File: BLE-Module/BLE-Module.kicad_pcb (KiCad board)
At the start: 2 copper layers, 50 x 31.4 mm, 20 parts, among them J1 USB-C

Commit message: Redesigned board
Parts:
- added C_OUT2: 22uF, Capacitor_SMD:C_1206_3216Metric, F.Cu at (190.9, 108.8)
- added ESP32_C_Power1: 22uF, Capacitor_SMD:C_1206_3216Metric, F.Cu at (168.9, 98.3)
- C_OUT1: value 52uF -> 22uF
- ESP32: value ESP32 -> ESP32-S3-MINI-1-N4R2
- moved J1 20.0 mm to (149.8, 106.6), turned to -90 degrees
- moved C3 12.9 mm to (159.4, 108.4)
- moved C4 12.9 mm to (159.4, 110.4)
- moved R4 12.9 mm to (159.4, 104.7)
- moved C_BYPASS1 12.9 mm to (159.4, 106.5)
- moved R3 11.1 mm to (159.4, 103.0), turned to 180 degrees
- moved BuckConverter1 11.1 mm to (161.1, 96.6), turned to 180 degrees
- moved R_FB_1 9.35 mm to (156.7, 94.8), turned to 90 degrees
- moved R_FB_2 4.68 mm to (190.9, 113.7), turned to 0 degrees
- moved R1 3.13 mm to (187.7, 113.9)
- moved ESP32 1.27 mm to (178.7, 101.6)
- moved C_OUT1 0.10 mm to (190.9, 111.5), turned to 0 degrees
- renumbered SW_BOOT1 to BOOT, SW_RST1 to RESET
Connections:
- net /+V_OUT renamed +3V3
- net VCC renamed +12V
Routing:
- net +3V3: track 63.4 -> 23.8 mm, vias 0 -> 7
- net /T1_IN: track 0.00 -> 22.5 mm
- net /R1_OUT: track 0.00 -> 19.1 mm
- net GND: track 0.00 -> 18.4 mm
- net Net-(UART-SERIAL1-V+): track 27.4 -> 12.7 mm, vias 2 -> 0
- net Net-(UART-SERIAL1-V-): track 30.0 -> 19.7 mm, vias 2 -> 0
- net /D+: track 19.9 -> 28.7 mm
- net /D-: track 19.6 -> 27.7 mm
- net Net-(J1-CC1): track 4.47 -> 8.30 mm
- net Net-(J1-CC2): track 10.0 -> 12.6 mm, vias 0 -> 2
- net /RESET: track 32.1 -> 30.6 mm
- net /LED: track 4.23 -> 3.27 mm
- net /BOOT: track 19.8 -> 20.0 mm, vias 0 -> 2

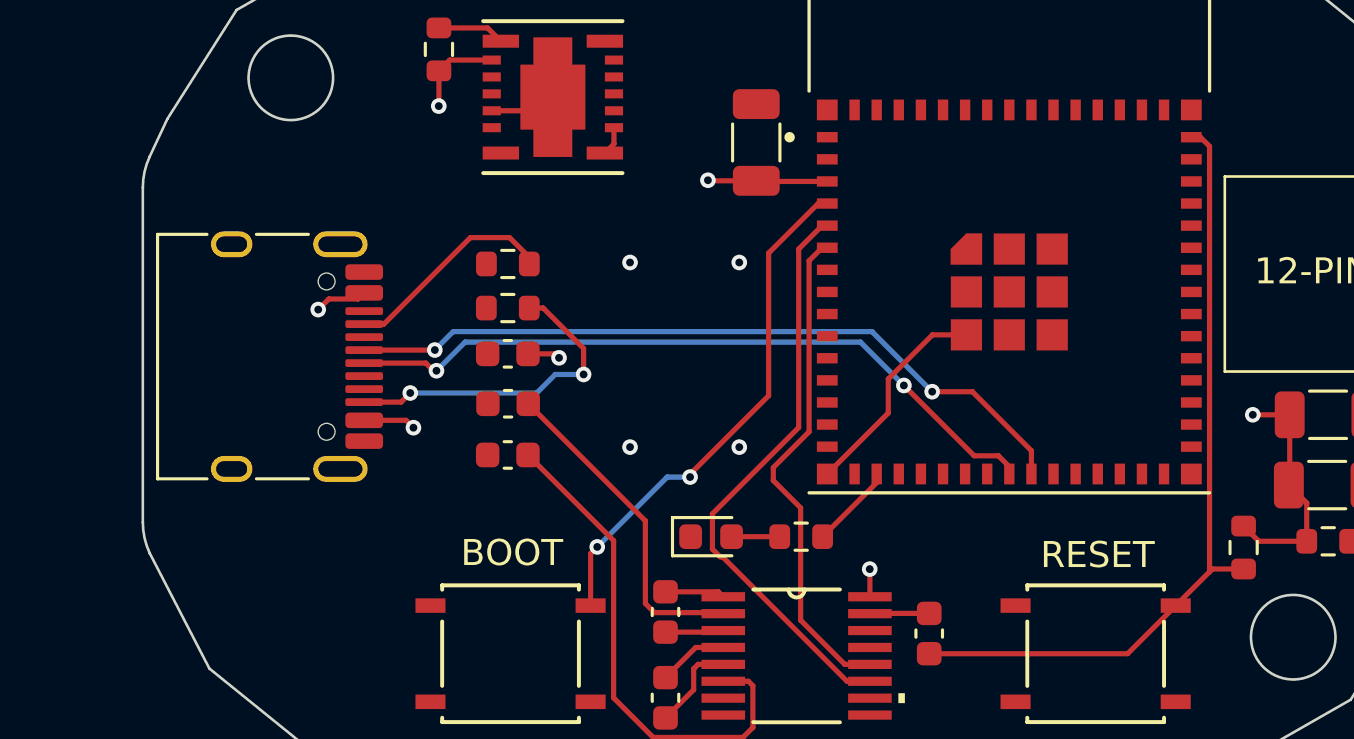
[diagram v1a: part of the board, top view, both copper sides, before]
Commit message: Picked USB-C receptacle
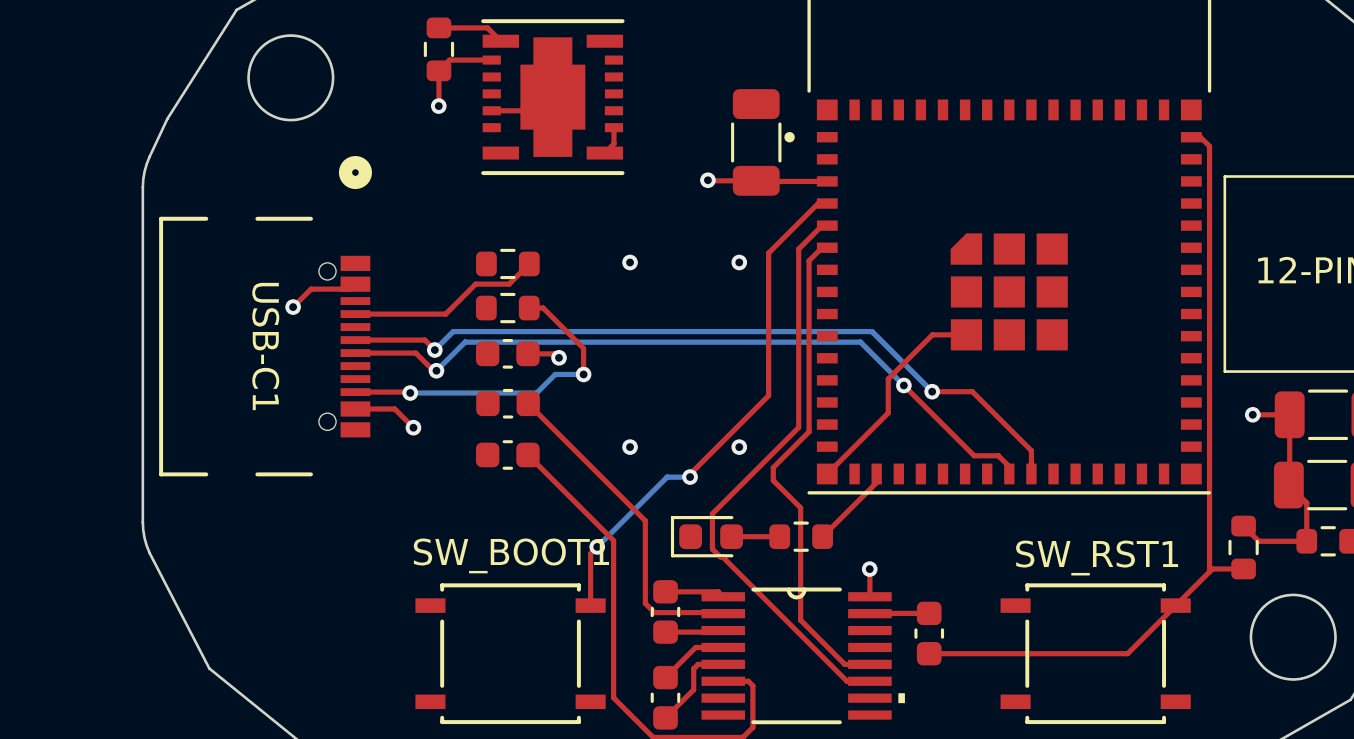
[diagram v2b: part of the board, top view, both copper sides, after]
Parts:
- removed J1: USB-C, Connector_USB:USB_C_Receptacle_HRO_TYPE-C-31-M-12
- added USB-C1: USB4105-GF-A, USB-C:USB4105_GCT, F.Cu at (150.1, 106.2)
- R2: value R -> 5.1K
- renumbered BOOT to SW_BOOT1, RESET to SW_RST1
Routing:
- net +3V3: track 23.8 -> 25.0 mm
- net Net-(USB-C1-CC1): track 8.30 -> 7.48 mm

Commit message: Added text and graphics
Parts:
- added G***: LOGO, LOGO, F.Cu at (152.0, 115.5)
- added G***: LOGO, LOGO, B.Cu at (170.7, 106.8)
- renumbered SW_BOOT1 to BOOT, SW_RST1 to RESET, USB-C1 to USB-C
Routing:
- net /RX_IN: track 0.00 -> 19.4 mm, vias 0 -> 3
- net +12V: track 1.12 -> 18.5 mm, vias 0 -> 3
- net /TX_OUT: track 0.00 -> 16.8 mm, vias 0 -> 3
- net GND: track 18.4 -> 22.8 mm, vias 0 -> 1
- net /BOOT: track 20.0 -> 20.5 mm
- net (no net): vias 4 -> 0
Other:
- board text added: "+12V"
- board text added: "GND"
- board text added: "RX"
- board text added: "TX"

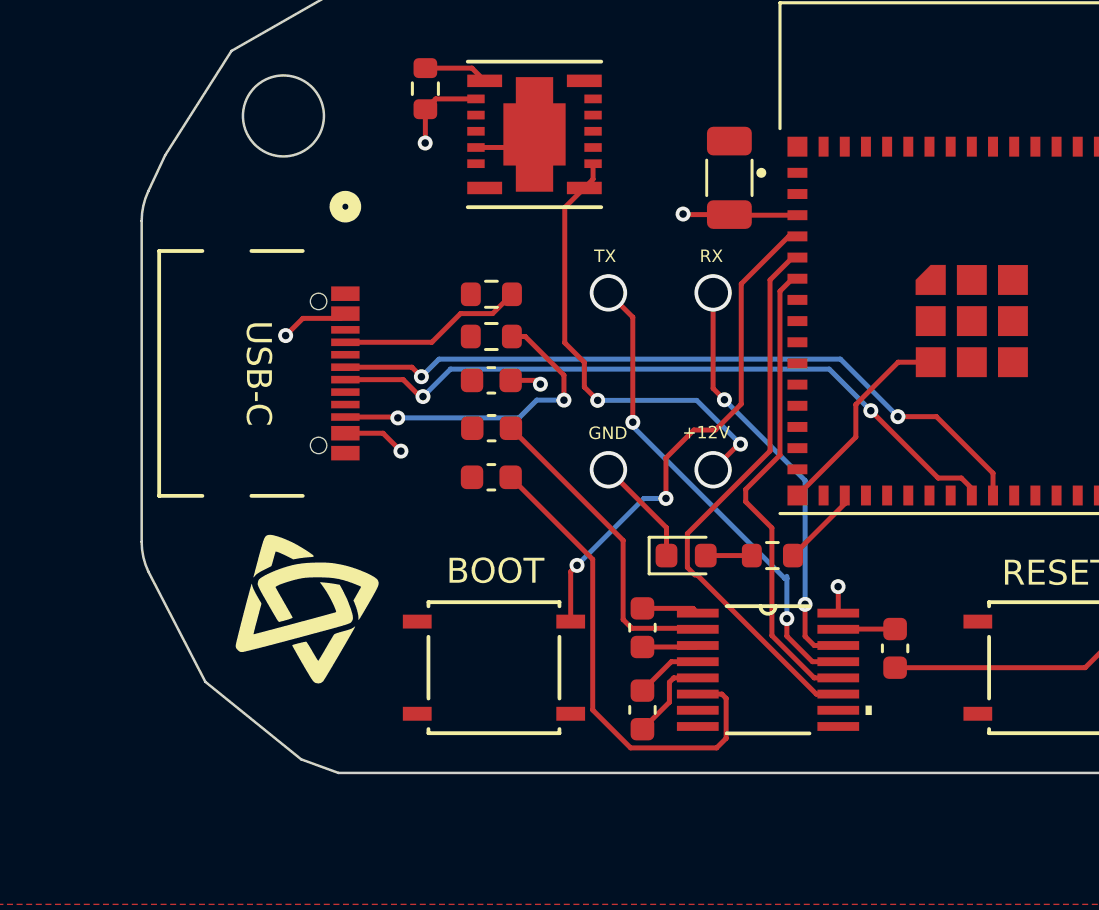
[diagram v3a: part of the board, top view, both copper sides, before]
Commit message: Added common-anode LED
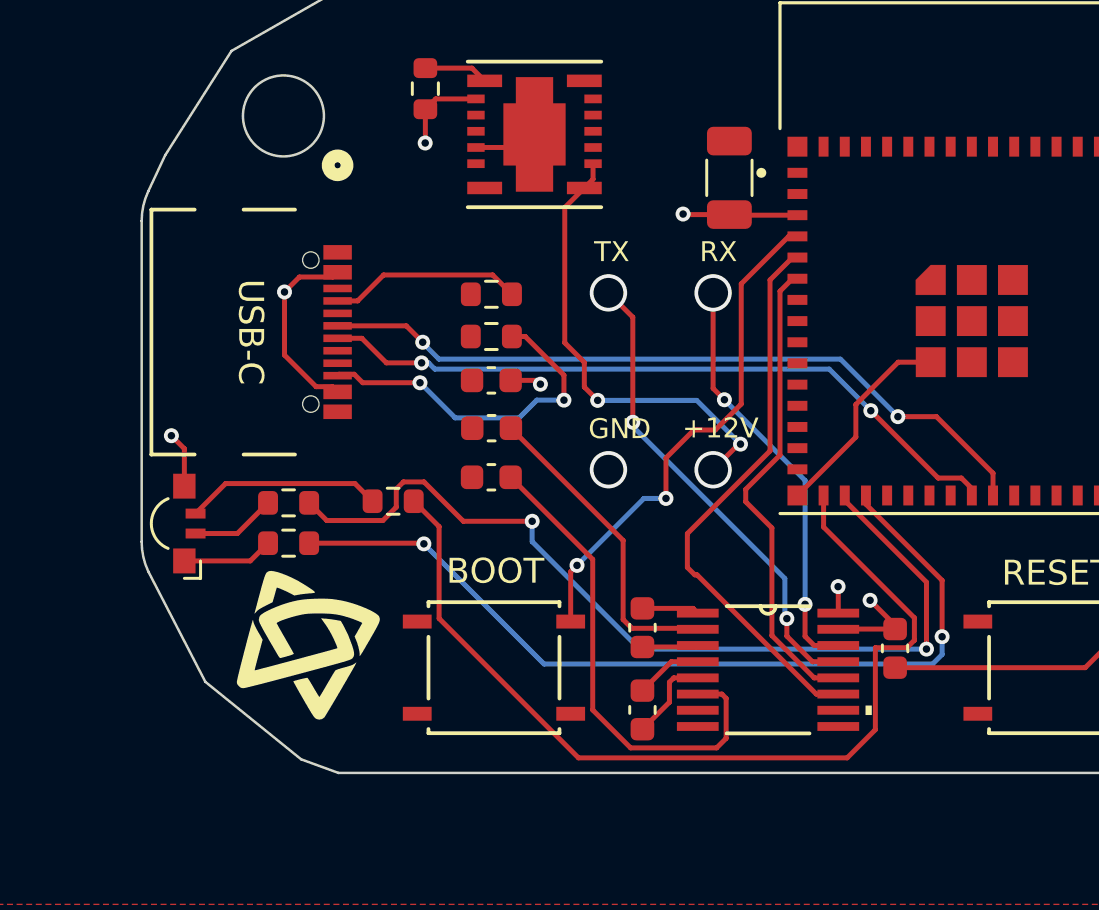
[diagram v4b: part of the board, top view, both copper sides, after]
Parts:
- removed D1: LED, LED_SMD:LED_0603_1608Metric
- removed R2: 5.1K, Resistor_SMD:R_0603_1608Metric
- added LED1: APFA3010, LED_SMD:LED_Kingbright_APFA3010_3x1.5mm_Horizontal, F.Cu at (147.1, 112.2)
- added R_BLUE1: 68, Resistor_SMD:R_0603_1608Metric, F.Cu at (151.3, 111.4)
- added R_GREEN1: 68, Resistor_SMD:R_0603_1608Metric, F.Cu at (155.5, 111.3)
- added R_RED1: 150, Resistor_SMD:R_0603_1608Metric, F.Cu at (151.3, 113.0)
- moved USB-C 1.69 mm to (149.7, 104.5)
- moved G*** 1.45 mm to (152.0, 117.0)
- moved G*** 1.41 mm to (169.5, 106.0)
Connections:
- ESP32 pad 16: unconnected-(ESP32-IO12-Pad16) -> /LED_GREEN
- ESP32 pad 17: /LED -> /LED_BLUE
- ESP32 pad 18: unconnected-(ESP32-IO14-Pad18) -> /LED_RED
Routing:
- net /LED_GREEN: track 0.00 -> 37.7 mm
- net /LED_BLUE: track 0.00 -> 36.9 mm, vias 0 -> 2
- net /LED_RED: track 0.00 -> 35.2 mm, vias 0 -> 2
- net Net-(LED1-G): track 0.00 -> 7.90 mm
- net +3V3: track 25.0 -> 29.7 mm
- net Net-(LED1-R): track 0.00 -> 3.65 mm
- net Net-(LED1-B): track 0.00 -> 3.42 mm
- net /LED: track 3.27 -> 0.00 mm
- net GND: track 22.8 -> 19.9 mm, vias 1 -> 2
- net Net-(D1-A): track 1.85 -> 0.00 mm
- net Net-(USB-C1-CC2): track 12.8 -> 13.9 mm

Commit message: updated docs
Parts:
- added +12V1: +12V, TestPoint:TestPoint_THTPad_2.5x2.5mm_Drill1.2mm, F.Cu at (168.3, 110.1)
- added GND1: GND, TestPoint:TestPoint_THTPad_2.5x2.5mm_Drill1.2mm, F.Cu at (164.1, 110.1)
- added RX1: TX_OUT, TestPoint:TestPoint_THTPad_2.5x2.5mm_Drill1.2mm, F.Cu at (168.3, 103.0)
- added TX1: RX_IN, TestPoint:TestPoint_THTPad_2.5x2.5mm_Drill1.2mm, F.Cu at (164.1, 103.0)
- R_BLUE1, R_GREEN1: value 68 -> 120
- R_RED1: value 150 -> 120
- renumbered USB-C to USB-C1
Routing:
- net GND: track 19.9 -> 26.9 mm, vias 2 -> 1
- net /T1_IN: track 22.5 -> 20.2 mm
- net /RX_IN: track 19.2 -> 20.2 mm, vias 3 -> 2
- net /R1_OUT: track 19.1 -> 18.2 mm
- net /BOOT: track 20.5 -> 21.3 mm
- net +12V: vias 3 -> 2
- net /TX_OUT: vias 3 -> 2

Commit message: Saving before I change the power plane
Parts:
- added 12_PIN1: FTSH-106-01-L-DV, 12_PIN:SAMTEC_FTSH-106-01-L-DV, F.Cu at (190.7, 102.5)
- renumbered BOOT to SW_BOOT1, RESET to SW_RST1
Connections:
- ESP32 pad 31: unconnected-(ESP32-IO35-Pad31) -> /MOSI
- ESP32 pad 32: unconnected-(ESP32-IO36-Pad32) -> /SCK
- ESP32 pad 33: unconnected-(ESP32-IO37-Pad33) -> /MISO
- ESP32 pad 34: unconnected-(ESP32-IO38-Pad34) -> /CS
- ESP32 pad 35: unconnected-(ESP32-IO39-Pad35) -> /IO_1
- ESP32 pad 36: unconnected-(ESP32-IO40-Pad36) -> /IO_2
- ESP32 pad 37: unconnected-(ESP32-IO41-Pad37) -> /IO_3
- ESP32 pad 38: unconnected-(ESP32-IO42-Pad38) -> /IO_4
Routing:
- net +12V: track 18.5 -> 43.2 mm, vias 2 -> 3
- net /IO_3: track 0.00 -> 15.4 mm, vias 0 -> 2
- net /IO_1: track 0.00 -> 15.2 mm, vias 0 -> 2
- net /IO_2: track 0.00 -> 15.1 mm, vias 0 -> 2
- net /IO_4: track 0.00 -> 14.7 mm, vias 0 -> 2
- net /MOSI: track 0.00 -> 11.9 mm
- net /SCK: track 0.00 -> 9.75 mm
- net /CS: track 0.00 -> 9.08 mm
- net GND: track 26.9 -> 36.0 mm, vias 1 -> 5
- net /MISO: track 0.00 -> 8.70 mm
- net +3V3: track 29.7 -> 34.2 mm
- net /RESET: track 30.6 -> 33.9 mm, vias 0 -> 2
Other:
- board text removed: "12-PIN"

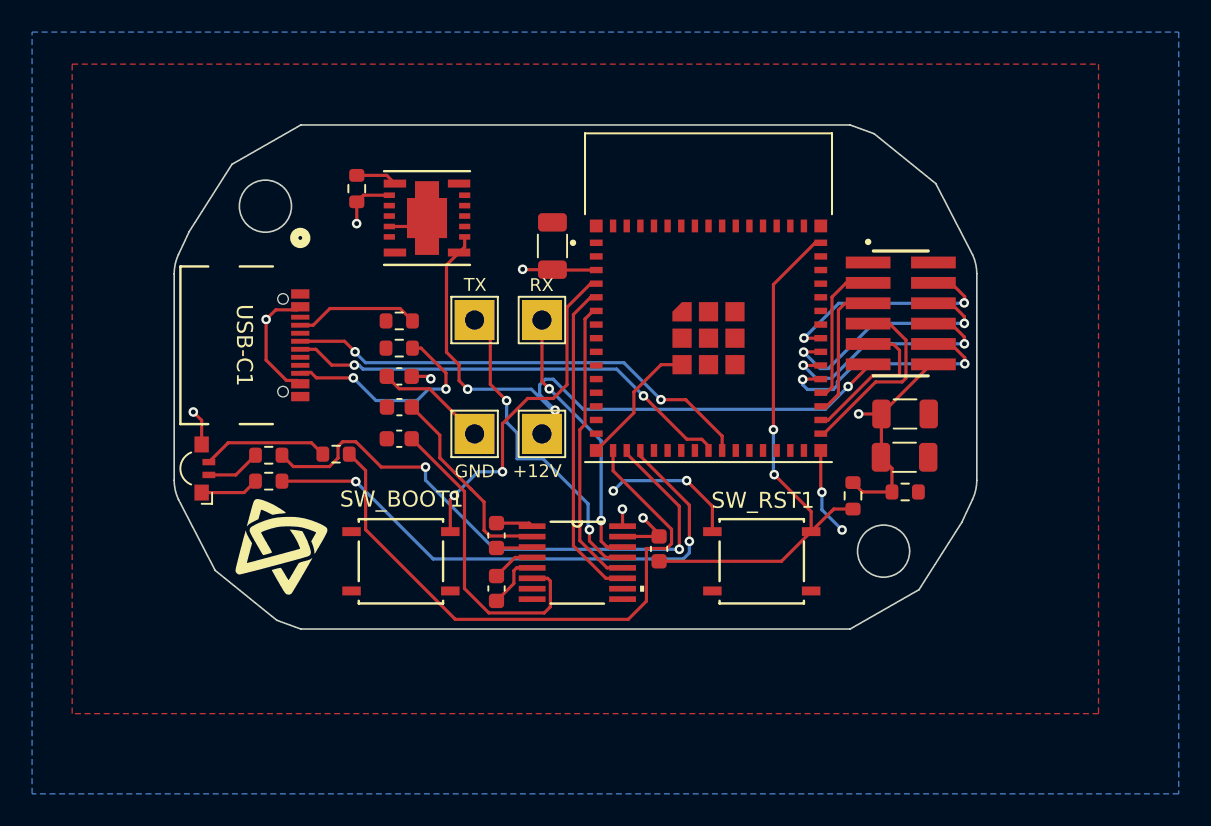
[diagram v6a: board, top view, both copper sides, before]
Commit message: Changed design to 4-layer
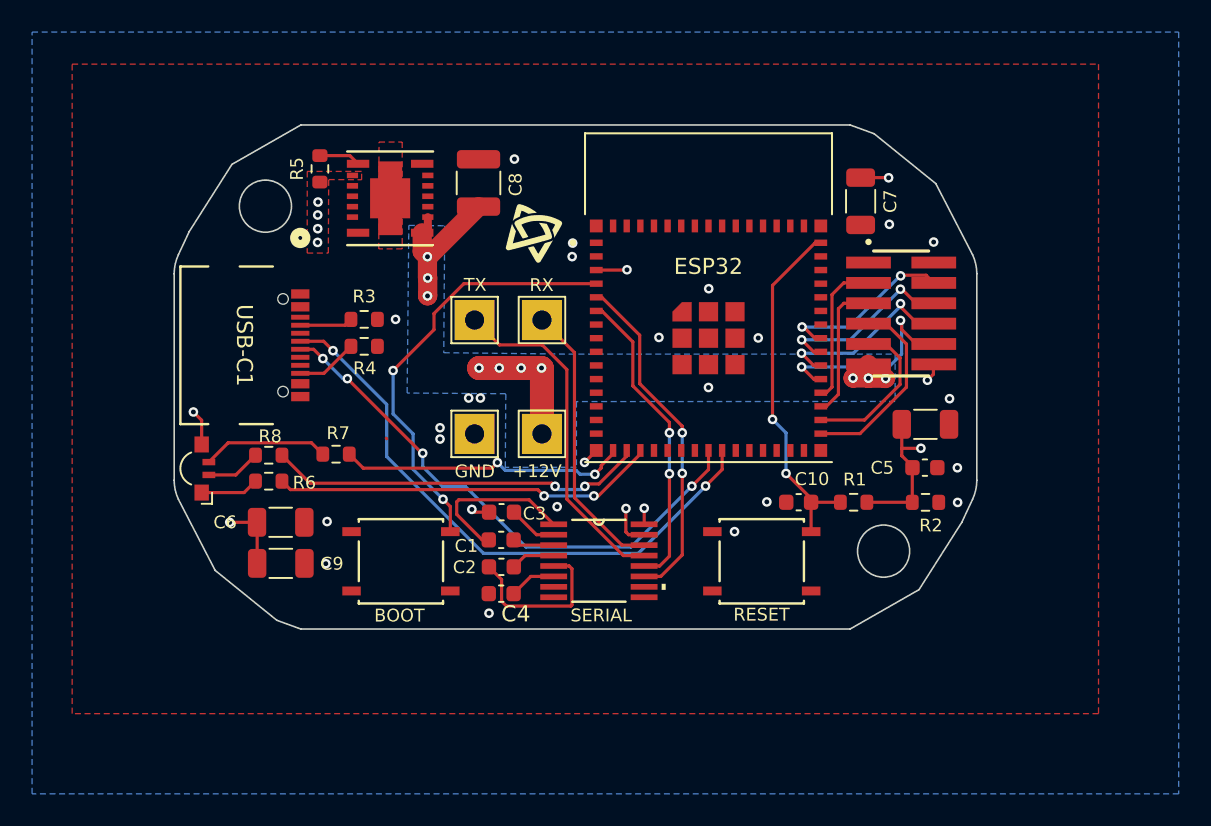
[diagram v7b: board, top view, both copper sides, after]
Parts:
- added C10: 1uF, Capacitor_SMD:C_0603_1608Metric, F.Cu at (184.3, 114.3)
- added C9: 22uF, Capacitor_SMD:C_1206_3216Metric, F.Cu at (152.0, 118.1)
- 12_PIN1: value FTSH-106-01-L-DV -> 12-PIN
- C5: renamed from C_OUT1; value 22uF -> 0.1uF; footprint Capacitor_SMD:C_1206_3216Metric -> Capacitor_SMD:C_0603_1608Metric
- C6: renamed from C_BYPASS1; value 0.1uF -> 22uF; footprint Capacitor_SMD:C_0603_1608Metric -> Capacitor_SMD:C_1206_3216Metric
- C8: renamed from C_Reset1; value 1uF -> 10uF; footprint Capacitor_SMD:C_0603_1608Metric -> Capacitor_SMD:C_1210_3225Metric
- SW_BOOT1: value SW_Push -> BOOT
- SW_RST1: value SW_Push -> RESET
- UART-SERIAL1: value TRSF3232EIPWR -> SERIAL
- moved C8 25.4 mm to (164.3, 94.4)
- moved G*** 25.1 mm to (167.8, 97.5)
- moved C7 19.4 mm to (188.2, 95.6)
- moved C6 11.7 mm to (152.0, 115.6), turned to 0 degrees
- moved C4 11.6 mm to (165.8, 120.0)
- moved C3 9.14 mm to (165.8, 114.9)
- moved BuckConverter 2.61 mm to (158.8, 95.4)
- moved R5 2.61 mm to (154.4, 93.5)
- moved R3 2.19 mm to (157.2, 102.9), turned to 0 degrees
- moved R4 2.19 mm to (157.2, 104.6), turned to 0 degrees
- moved C5 1.42 mm to (192.2, 112.2)
- moved C_OUT2 1.42 mm to (192.2, 109.5)
- moved R2 1.42 mm to (192.2, 114.3)
- moved C2 1.38 mm to (165.8, 118.3), turned to 0 degrees
- moved UART-SERIAL1 1.35 mm to (171.8, 118.0)
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- renumbered BuckConverter1 to BuckConverter, ESP32_C_Power1 to C7, R_FB_2 to R2, R_FB_1 to R5, R_RED1 to R6, R_GREEN1 to R7, R_BLUE1 to R8
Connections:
- C7 pad 1: GND -> +3V3
- C7 pad 2: +3V3 -> GND
- C8 pad 1: /RESET -> +12V
- USB-C1 pad A4-B9: +3V3 -> unconnected-(USB-C1-VBUS-PadA4-B9)
- USB-C1 pad B4-A9: +3V3 -> unconnected-(USB-C1-VBUS-PadB4-A9)
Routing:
- net GND: track 36.0 -> 4.91 mm, vias 5 -> 26
- net +12V: track 43.2 -> 20.6 mm, vias 3 -> 10
- net /LED_GREEN: track 37.7 -> 18.1 mm, vias 0 -> 2
- net Net-(UART-SERIAL1-V-): track 19.7 -> 2.94 mm
- net /LED_BLUE: track 36.9 -> 23.6 mm
- net +3V3: track 34.2 -> 21.5 mm, vias 7 -> 11
- net /RESET: track 33.9 -> 22.3 mm
- net /LED_RED: track 35.2 -> 24.0 mm
- net Net-(USB-C1-CC2): track 13.9 -> 3.86 mm, vias 2 -> 0
- net Net-(UART-SERIAL1-V+): track 12.7 -> 3.06 mm
- net Net-(UART-SERIAL1-C1+): track 2.30 -> 10.2 mm
- net /D+: track 29.7 -> 37.0 mm
- net Net-(UART-SERIAL1-C2-): track 3.55 -> 10.5 mm
- net /D-: track 28.2 -> 34.2 mm, vias 2 -> 4
- net /BOOT: track 21.3 -> 27.0 mm
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- added copper zone on B.Cu, net +12V
- added copper zone on F.Cu, net +3V3
- added copper zone on In1.Cu, net GND
- added copper zone on In2.Cu, net GND
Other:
- copper layers 2 -> 4
